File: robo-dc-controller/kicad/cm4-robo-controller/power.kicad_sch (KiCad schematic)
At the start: 27 parts, among them Q10 NCE6008AS, Q11 BSS138, Q9 DMP6023LE-13, SW3 SS-12F49-G050, U17 MX26631DL

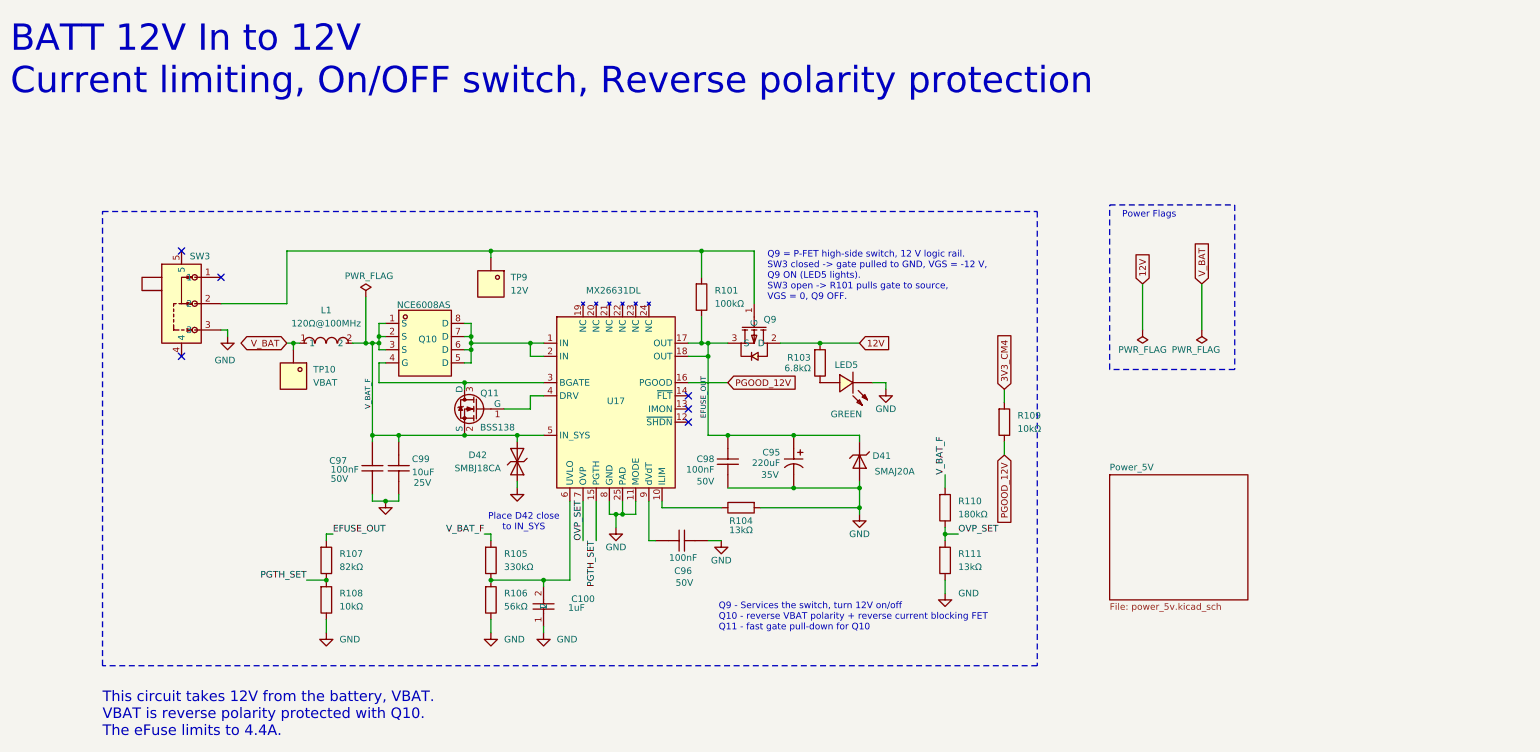
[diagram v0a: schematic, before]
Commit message: CM4 carrier: GPS sheet integration, U12 expansion header, power fixes
Populate U12 (2x12 expansion header) on the CM4_Connectors sheet:
all 19 CM4 signals plus 3V3_CM4 and four grounds, with 2.2k I2C
pull-ups (R113/R114) on GPIO2/GPIO3. Value matches the CM4IO
reference design, which uses 2.2k on SDA1/SCL1.

Wire the new GPS sheet (MAX-M10S) into the CM4 sheet: add sheet pins
for GPS_RX_MCU, GPS_TX_MCU and 1PPS_MCU. The UART lands on UART3
(GPIO4 = TXD3 to the GPS RXD, GPIO5 = RXD3 from the GPS TXD) and
1PPS on GPIO16. Needs dtoverlay=uart3 in config.txt. The leftover
CM4_TX/CM4_RX/1PPS_MCU hierarchical labels, which pointed at a root
sheet with no matching pins, become local labels on those nets.

Fix the orphaned 3V3 label on the GPS sheet, which left the MS621FE
backup cell with no charge path, and scope 3V3_CM4 to the CM4
hierarchy: local labels in the CM4 sheet, hierarchical labels plus
sheet pins in each consuming sub-sheet. Net membership is unchanged
at 30 nodes.

Add PWR_FLAGs on the 5V rail and on GND. Both are driven through
passive parts (an inductor and ground symbols respectively), so ERC
could not see a driver.

ERC: 55 -> 40 violations. Of the remainder, 30 are the RoboClaw U1,
which is placed on the root sheet but not yet wired.
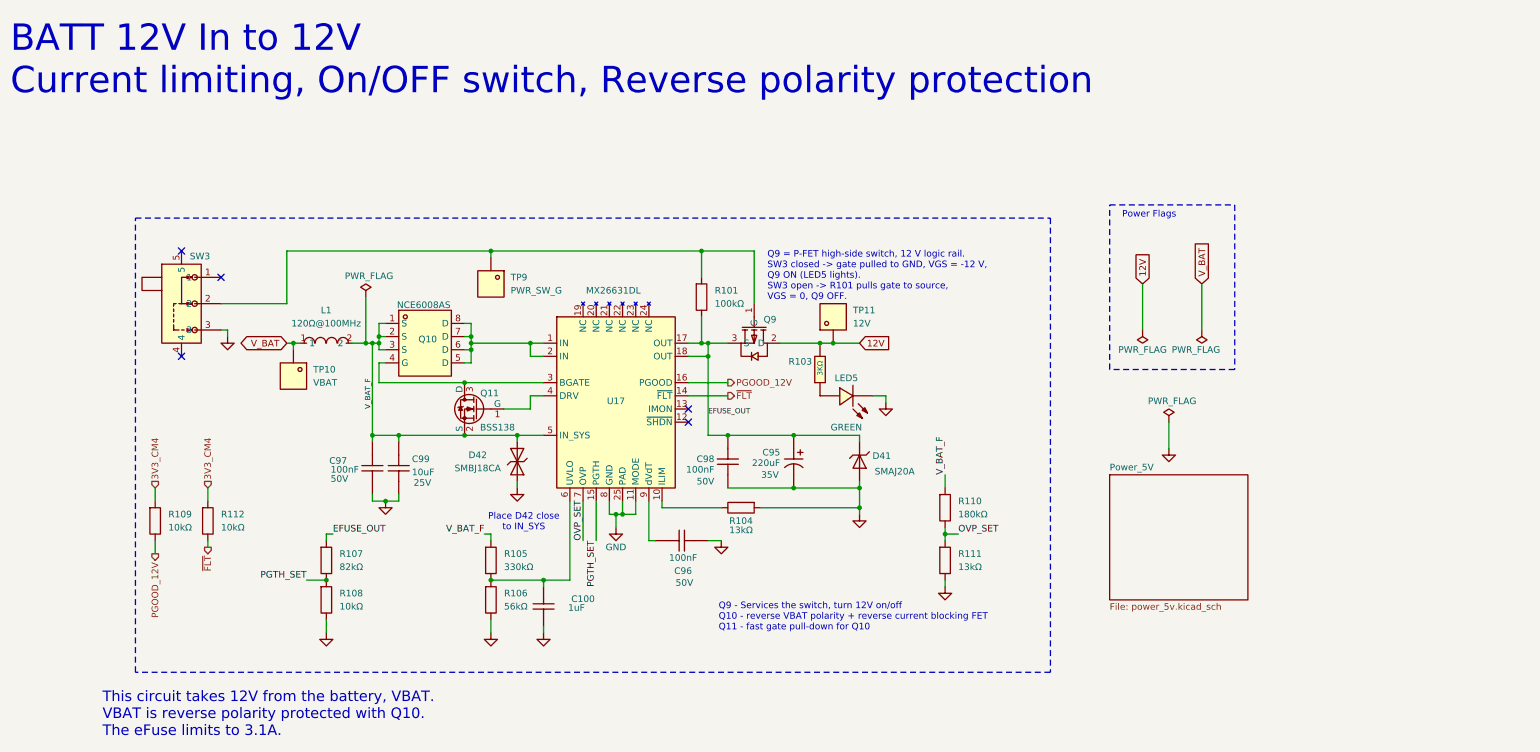
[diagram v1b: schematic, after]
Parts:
- removed R103: 6.8kΩ, PCM_JLCPCB:R_0603, symbol PCM_JLCPCB-Resistors:0603,6.8kΩ
- added R103: 3KΩ, MyParts:R0603, symbol MyParts:0603WAF3001T5E
- added R112: 10kΩ, PCM_JLCPCB:R_0603, symbol PCM_JLCPCB-Resistors:0603,10kΩ
- added TP11: 12V, MyParts:TESTPOINT-SMD_L3.0-W2.0, symbol MyParts:RH-5016
- D41: Attrition Qty 4 -> 2; Breakdown Voltage 19.7V -> 24.5V; Maximum Clamping Voltage 26V -> 32.4V; Price 0.038USD -> 0.037USD; Reverse Stand-Off Voltage (Vrwm) 16V -> 20V; Stock 7028 -> 8843
- R110: Stock 51181774 -> 453075
- R111: LCSC C25804 -> C22797; Stock 51181774 -> 264187
- TP9: value 12V -> PWR_SW_G
- U17: LCSC (none) -> C18197523
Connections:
- net 12V: now also R103.2, TP11.1
- net 3V3_CM4: now also R112.1
- net at LED5.1 (A): now also R103.1
- net ~{FLT}: now reaches U17.14 (~{FLT})
- net ~{FLT}: now also R112.2
- no-connect marks 6 -> 5
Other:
- note added: "This circuit takes 12V from the battery, VBAT. VBAT is reverse polarity protected with Q10. The eFuse limits to 3.1A."
- note removed: "This circuit takes 12V from the battery, VBAT. VBAT is reverse polarity protected with Q10. The eFuse limits to 4.4A."
- moved on the sheet: LED5, R109
